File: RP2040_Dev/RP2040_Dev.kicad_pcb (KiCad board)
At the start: 2 copper layers, 40 parts, among them J1 USB4105-GF-A, J2 Conn_01x18_Pin, J3 Conn_01x18_Pin, SW1 SW_Push, SW2 SW_Push, U1 RP2040, U2 W25Q128JVS, U4 AMS1117CS-3.3, Y1 ABM8G-12.000MHZ-4Y-T3

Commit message: rp2040 update
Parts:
- C1, C10, C11, C12, C16, C17, C2, C3, C4, C5, C7, C8, C9: footprint Capacitor_SMD:C_0402_1005Metric_Pad0.74x0.62mm_HandSolder -> Capacitor_SMD:C_0201_0603Metric_Pad0.64x0.40mm_HandSolder
- C13, C14, C15, C6: footprint Capacitor_SMD:C_0402_1005Metric_Pad0.74x0.62mm_HandSolder -> Capacitor_SMD:C_0201_0603Metric_Pad0.64x0.40mm_HandSolder; moved to B.Cu
- R1, R10, R2, R3, R4, R5, R6, R7, R8, R9: footprint Resistor_SMD:R_0402_1005Metric_Pad0.72x0.64mm_HandSolder -> Resistor_SMD:R_0201_0603Metric_Pad0.64x0.40mm_HandSolder
- moved R5 55.6 mm to (114.8, 84.8)
- moved C3 54.2 mm to (107.9, 82.8), turned to -90 degrees
- moved C8 52.6 mm to (117.9, 68.5)
- moved C7 49.1 mm to (117.9, 65.0)
- moved R6 49.0 mm to (109.5, 82.8), turned to -90 degrees
- moved C16 48.0 mm to (113.9, 74.3), turned to -90 degrees
- moved C10 47.3 mm to (113.0, 71.4), turned to -90 degrees
- moved C15 46.5 mm to (112.8, 70.8), turned to -90 degrees
- moved C4 46.3 mm to (107.8, 73.3)
- moved C6 43.7 mm to (112.7, 60.9), turned to 90 degrees
- moved C9 42.5 mm to (107.2, 68.5), turned to 180 degrees
- moved C12 41.8 mm to (109.7, 71.4), turned to -90 degrees
- moved C17 40.5 mm to (107.8, 72.3)
- moved C5 40.4 mm to (107.2, 65.0), turned to 180 degrees
- moved C11 40.4 mm to (106.8, 70.7)
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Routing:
- net +3.3V: track 0.00 -> 17.2 mm
- net VBUS: track 0.00 -> 5.26 mm
- net Net-(F1-Pad1): track 0.00 -> 5.04 mm
- net Net-(J1-CC1): track 0.00 -> 3.66 mm
- net GND: vias 0 -> 1
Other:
- copper layers 2 -> 14

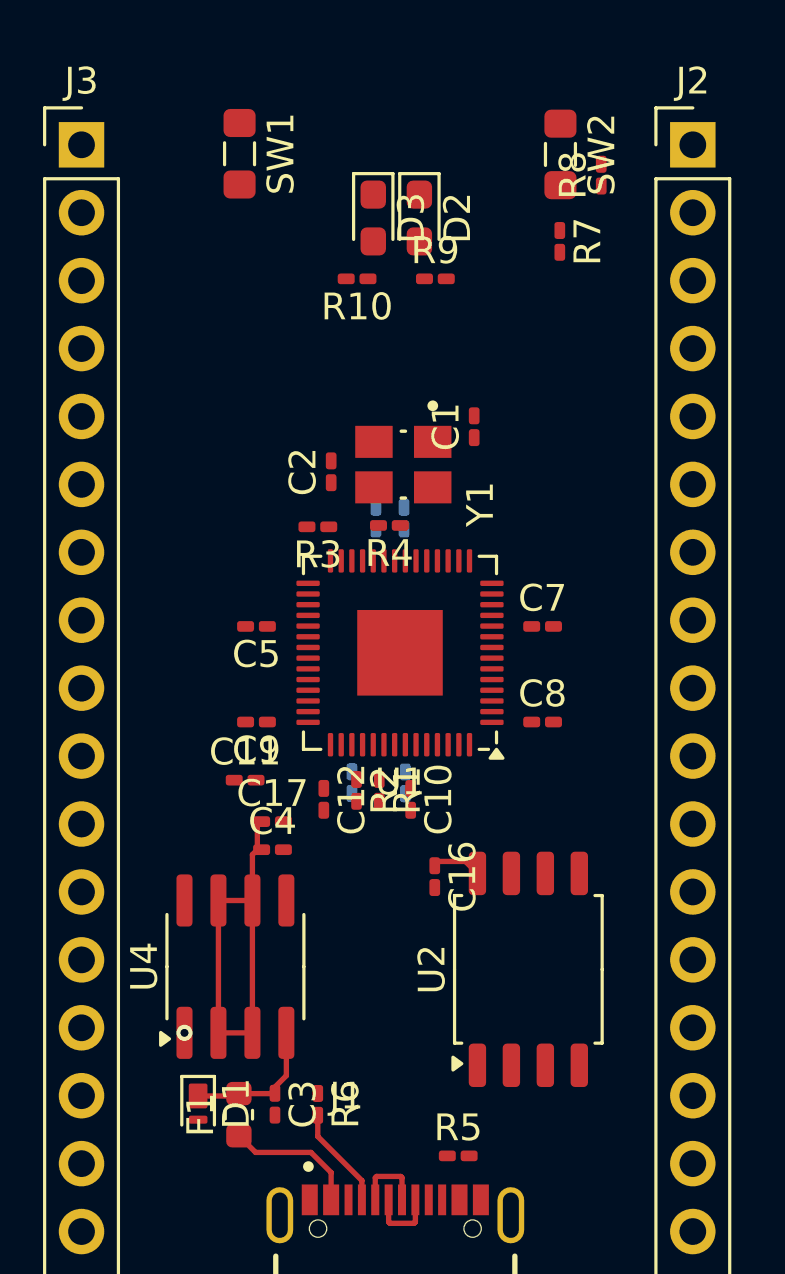
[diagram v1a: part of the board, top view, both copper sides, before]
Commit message: Adjusted Headers on ATmega32
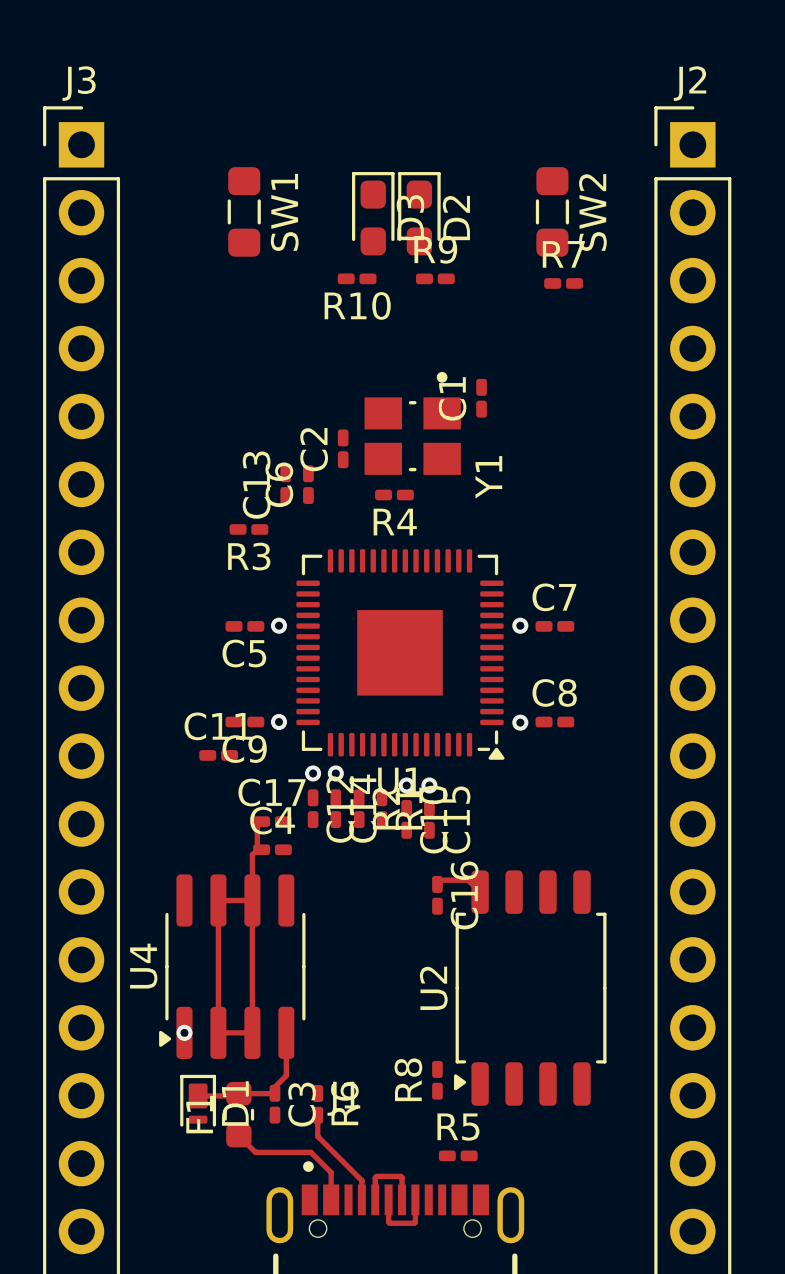
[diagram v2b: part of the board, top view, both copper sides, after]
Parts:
- C13, C14, C15, C6: moved to F.Cu
- moved R8 34.4 mm to (114.0, 82.0)
- moved C6 3.79 mm to (109.2, 59.7)
- moved C13 3.60 mm to (108.3, 59.7)
- moved R3 2.58 mm to (106.9, 61.4)
- moved SW1 2.18 mm to (106.8, 49.5)
- moved SW2 2.17 mm to (118.3, 49.5)
- moved C15 1.64 mm to (113.7, 72.2)
- moved R7 1.58 mm to (118.7, 52.1), turned to 0 degrees
- moved C11 1.35 mm to (105.8, 69.8)
- moved R4 1.16 mm to (112.4, 60.1)
- moved C14 1.14 mm to (110.2, 71.8)
- moved Y1 1.12 mm to (113.0, 57.9)
- moved C1 1.10 mm to (115.6, 56.4)
- moved C2 0.97 mm to (110.5, 58.3)
- moved C10 0.76 mm to (112.8, 72.2)
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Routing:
- net (no net): vias 0 -> 8

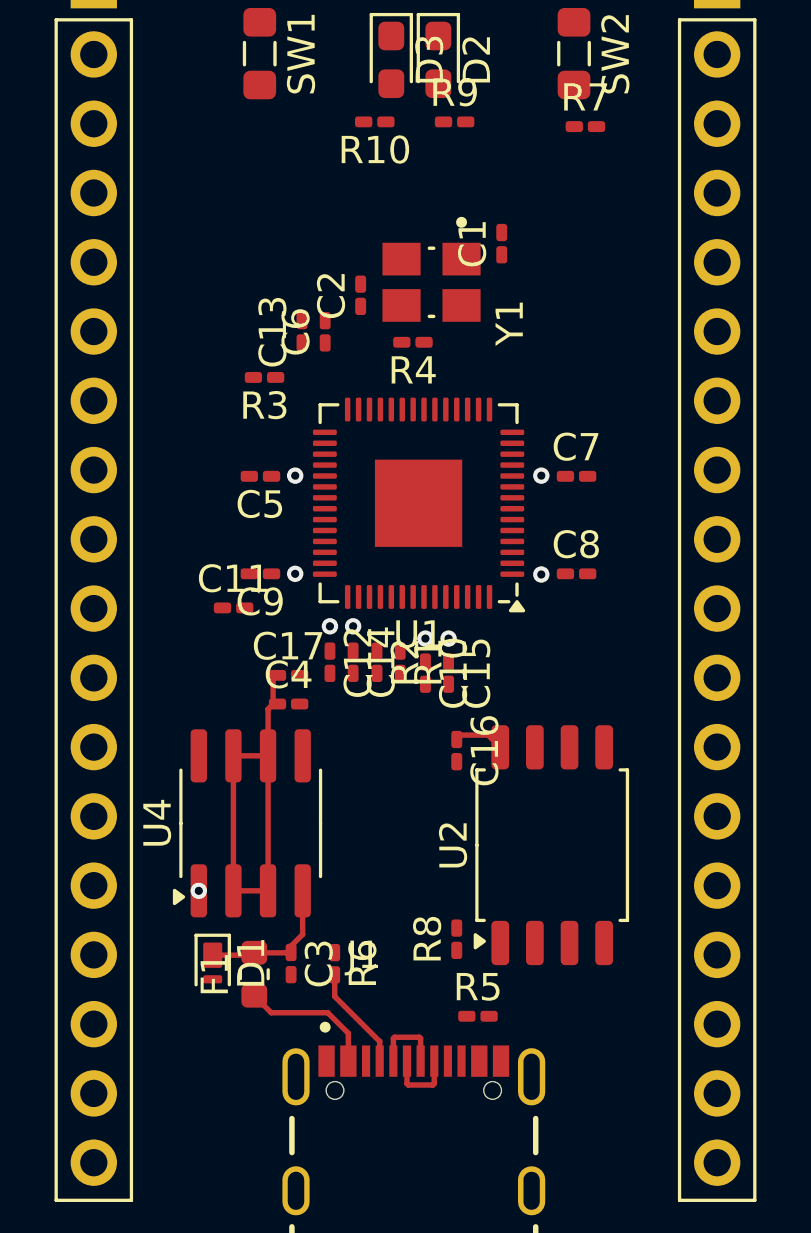
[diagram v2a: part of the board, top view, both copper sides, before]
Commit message: Cleaned up atmega and made atmega32 README
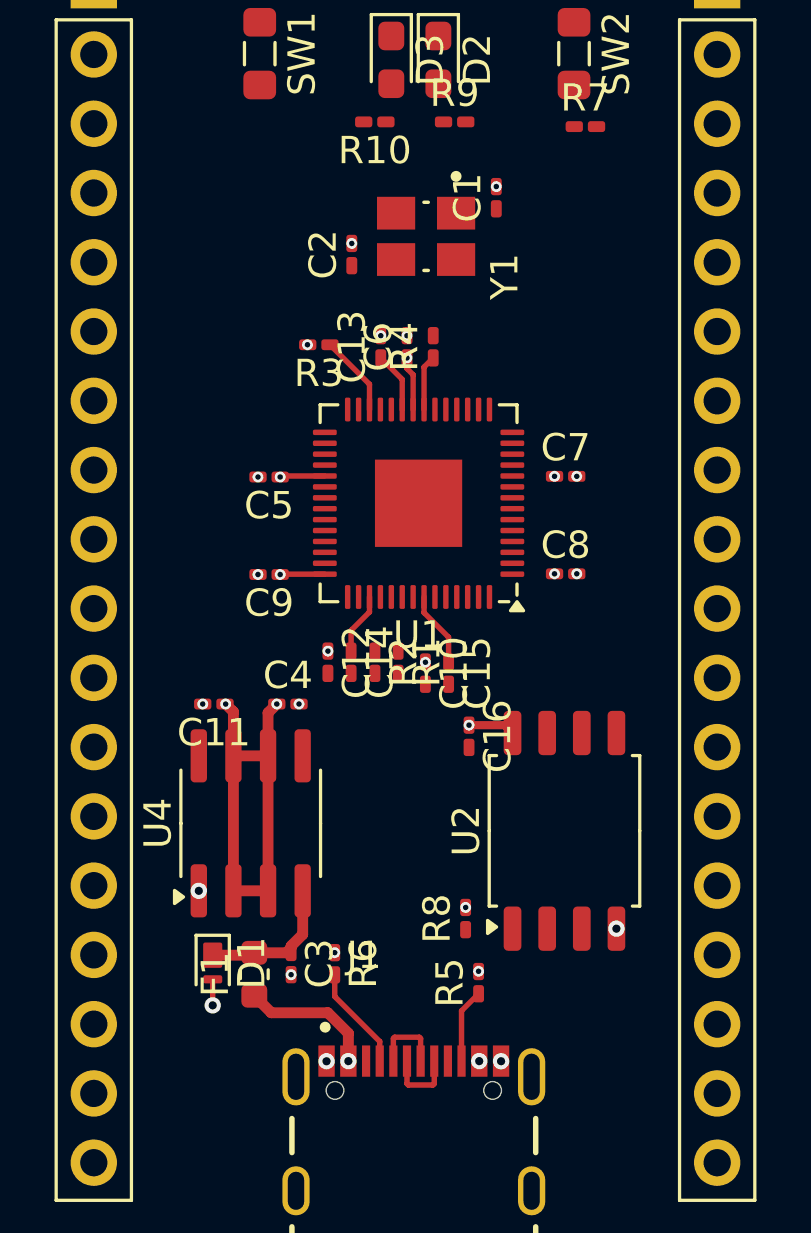
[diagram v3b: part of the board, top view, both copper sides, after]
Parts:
- removed the C11 at (105.8, 69.8)
- moved C6 3.05 mm to (112.2, 60.2)
- moved C13 2.94 mm to (111.2, 60.2)
- moved C11 2.93 mm to (105.1, 73.3), turned to 180 degrees
- moved R3 2.33 mm to (108.9, 60.1)
- moved C1 1.70 mm to (115.4, 54.8)
- moved Y1 1.70 mm to (112.8, 56.2)
- moved C2 1.53 mm to (110.1, 56.8)
- moved R5 1.23 mm to (114.8, 83.5), turned to 90 degrees
- moved R8 0.82 mm to (114.3, 81.2)
- moved R4 0.76 mm to (113.1, 60.2), turned to 90 degrees
- moved C16 0.69 mm to (114.4, 74.5)
- moved U2 0.69 mm to (117.9, 78.0)
- moved C7 0.40 mm to (118.0, 65.0)
- moved C8 0.40 mm to (118.0, 68.5)
- moved C5 0.32 mm to (107.1, 65.0)
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- renumbered C17 to C11
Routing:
- net +1V1: track 0.00 -> 7.24 mm
- net +3.3V: track 17.2 -> 23.5 mm, vias 0 -> 12
- net /RUN: track 0.00 -> 2.98 mm
- net Net-(J1-CC2): track 0.00 -> 2.73 mm
- net /Xout: track 0.00 -> 2.03 mm
- net GND: track 0.00 -> 0.95 mm, vias 1 -> 18
- net Net-(F1-Pad1): vias 0 -> 2
- net (no net): vias 8 -> 0

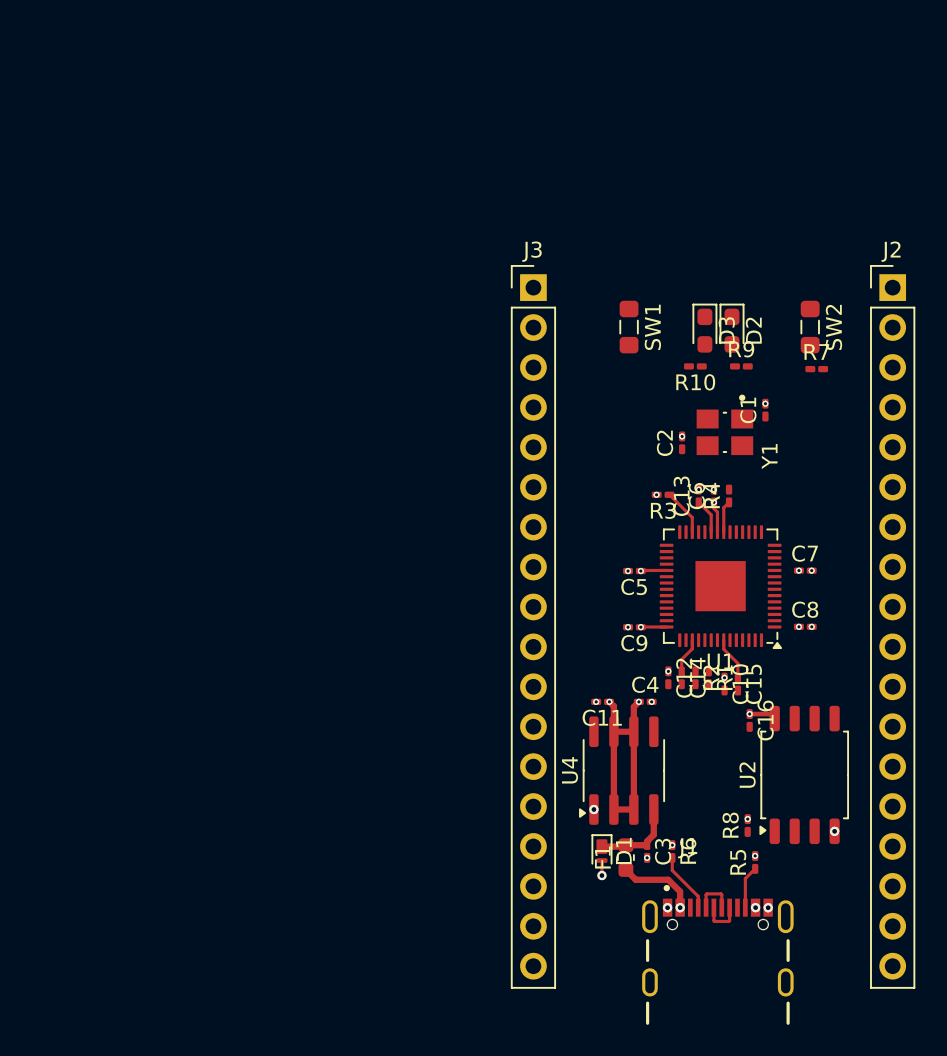
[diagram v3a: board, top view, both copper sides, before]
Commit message: Added additional board folders, updataed RP2040, ATmega, and ESP32
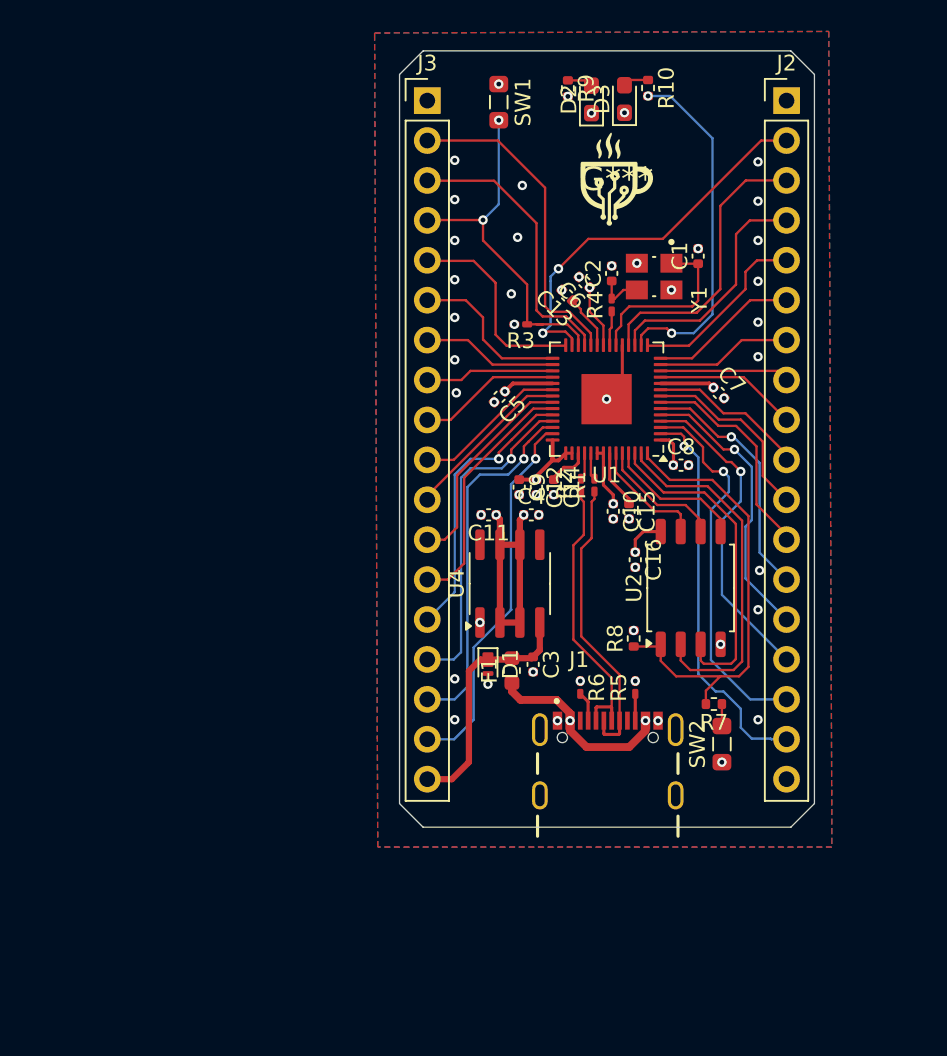
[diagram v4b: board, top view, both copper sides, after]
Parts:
- added G***: LOGO, Footprints:6mm Coffee, F.Cu at (106.0, 40.1)
- C1, C10, C11, C12, C13, C14, C15, C16, C2, C3, C4, C5, C6, C7, C8, C9: footprint Capacitor_SMD:C_0201_0603Metric_Pad0.64x0.40mm_HandSolder -> Capacitor_SMD:C_0402_1005Metric
- R10, R7, R8, R9: footprint Resistor_SMD:R_0201_0603Metric_Pad0.64x0.40mm_HandSolder -> Resistor_SMD:R_0402_1005Metric
- moved SW2 27.1 mm to (112.7, 76.0), turned to 90 degrees
- moved R7 22.3 mm to (112.1, 73.5), turned to 180 degrees
- moved R9 20.9 mm to (102.9, 34.3), turned to -90 degrees
- moved R10 18.0 mm to (108.0, 34.3), turned to -90 degrees
- moved D2 17.2 mm to (104.4, 35.0), turned to 90 degrees
- moved SW1 16.5 mm to (98.5, 35.2)
- moved C6 15.9 mm to (103.9, 46.6), turned to 135 degrees
- moved D3 15.6 mm to (106.5, 35.0), turned to 90 degrees
- moved C13 15.3 mm to (102.8, 47.5), turned to 135 degrees
- moved C12 14.8 mm to (100.9, 59.7)
- moved C14 14.6 mm to (102.0, 59.7)
- moved R4 14.3 mm to (105.6, 48.1)
- moved R1 14.3 mm to (104.5, 59.5), turned to 90 degrees
- moved R2 14.3 mm to (103.7, 59.5), turned to 90 degrees
- moved R3 14.1 mm to (99.9, 49.3)
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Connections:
- J2 pad 10: /GPIO24 -> /GPIO7
- J2 pad 11: /GPIO25 -> /GPIO6
- J2 pad 12: /GPIO26 -> /GPIO5
- J2 pad 13: /GPIO27 -> /GPIO4
- J2 pad 14: /GPIO28 -> /GPIO3
- J2 pad 15: /GPIO29 -> /GPIO2
- J2 pad 16: /SWCLK -> /GPIO1
- J2 pad 17: /SWD -> /GPIO0
- J2 pad 3: /GPIO17 -> /GPIO15
- J2 pad 4: /GPIO18 -> /GPIO14
- J2 pad 5: /GPIO19 -> /GPIO12
- J2 pad 6: /GPIO20 -> /GPIO11
- J2 pad 7: /GPIO21 -> /GPIO10
- J2 pad 8: /GPIO22 -> /GPIO9
- J2 pad 9: /GPIO23 -> /GPIO8
- J3 pad 1: VBUS -> GND
- J3 pad 10: /GPIO8 -> /GPIO22
- J3 pad 11: /GPIO9 -> /GPIO23
- J3 pad 12: /GPIO10 -> /GPIO24
- J3 pad 13: /GPIO11 -> /GPIO25
- J3 pad 14: /GPIO12 -> /GPIO26
- J3 pad 15: /RUN -> /GPIO27
- J3 pad 16: /GPIO14 -> /GPIO28
- J3 pad 17: /GPIO15 -> /GPIO29
- J3 pad 18: GND -> VBUS
- J3 pad 2: /GPIO0 -> /SWCLK
- J3 pad 3: /GPIO1 -> /SWD
- J3 pad 4: /GPIO2 -> /RUN
- J3 pad 5: /GPIO3 -> /GPIO17
- J3 pad 6: /GPIO4 -> /GPIO18
- J3 pad 7: /GPIO5 -> /GPIO19
- J3 pad 8: /GPIO6 -> /GPIO20
- J3 pad 9: /GPIO7 -> /GPIO21
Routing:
- net /QSPI_SS: track 0.00 -> 29.1 mm
- net /GPIO0: track 0.00 -> 25.2 mm, vias 0 -> 1
- net /GPIO16: track 0.00 -> 24.9 mm, vias 0 -> 2
- net /GPIO1: track 0.00 -> 24.2 mm, vias 0 -> 1
- net /GPIO29: track 0.00 -> 24.1 mm, vias 0 -> 1
- net /GPIO28: track 0.00 -> 23.0 mm, vias 0 -> 1
- net /QSPI_SD1: track 0.00 -> 22.9 mm
- net /GPIO13: track 0.00 -> 22.4 mm, vias 0 -> 2
- net /GPIO27: track 0.00 -> 21.1 mm, vias 0 -> 1
- net /QSPI_SD2: track 0.00 -> 20.8 mm
- net /SWCLK: track 0.00 -> 20.7 mm
- net /GPIO2: track 0.00 -> 20.6 mm, vias 0 -> 1
- net /RUN: track 2.98 -> 22.7 mm, vias 0 -> 2
- net /GPIO15: track 0.00 -> 18.3 mm
- net /GPIO3: track 0.00 -> 18.1 mm, vias 0 -> 1
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- added copper zone on In2.Cu, net +3.3V
- added copper zone on B.Cu, net GND
- added copper zone on F.Cu, net GND
- added copper zone on In1.Cu, net GND
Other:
- board outline added: 26.4 x 49.4 mm
- copper layers 14 -> 4
